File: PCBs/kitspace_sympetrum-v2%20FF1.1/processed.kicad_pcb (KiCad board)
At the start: 2 copper layers, 98.8 x 77.3 mm, 67 parts, among them SW101 DFU, U101 STM32F030K6T6, U102 TSSP58P38, U201 APA102_5050, U202 APA102_5050, U203 APA102_5050, U204 APA102_5050, U205 APA102_5050, U206 APA102_5050, U207 APA102_5050, U208 APA102_5050, U209 APA102_5050, U210 APA102_5050, U301 AAT1217-3.3

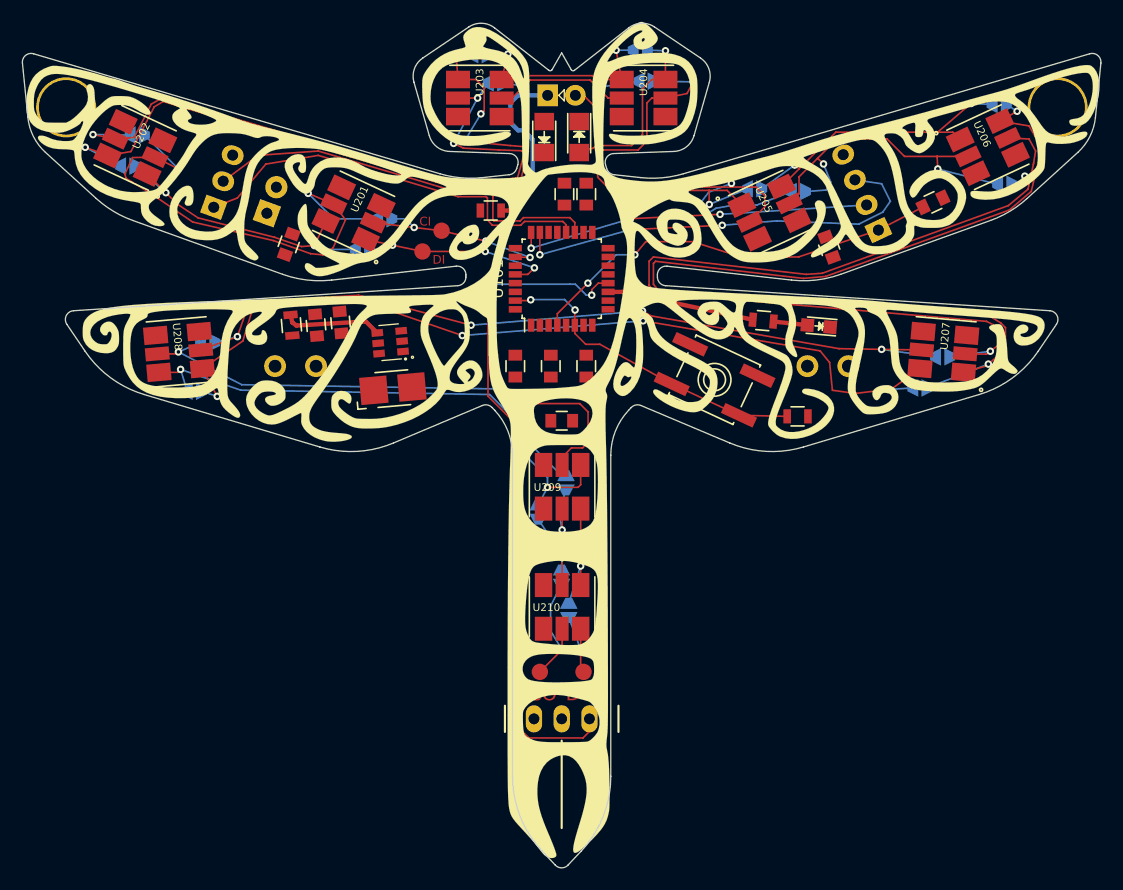
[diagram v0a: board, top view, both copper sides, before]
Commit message: recheck all circuits and clean up fill zone by rerouting the nets using freerouting and manually
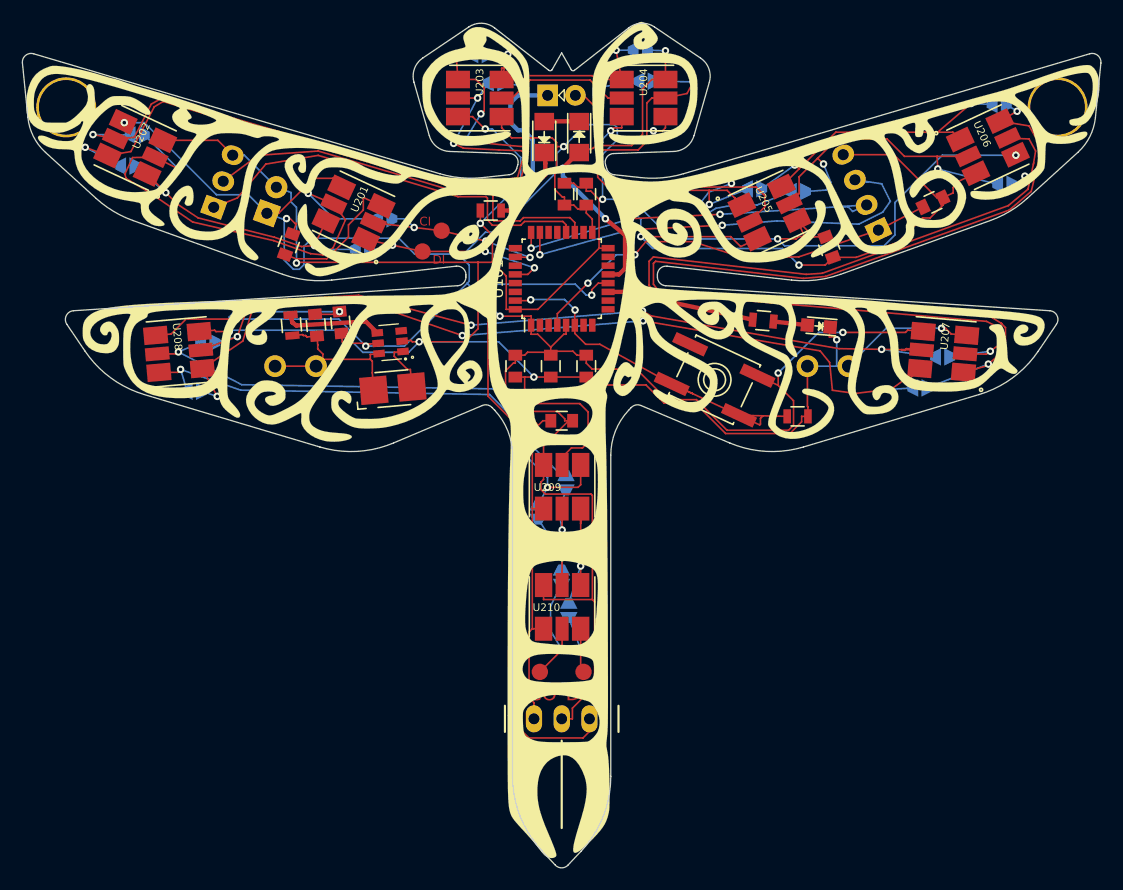
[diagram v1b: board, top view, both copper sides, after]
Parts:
- renumbered G*** to G***_2, G*** to G***_3
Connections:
- B301 pad 1: (no net) -> +BATT
- B301 pad 2: (no net) -> GND
- C101 pad 2: (no net) -> GND
- C102 pad 1: (no net) -> +3V3
- C102 pad 2: (no net) -> GND
- C103 pad 1: (no net) -> +3V3
- C103 pad 2: (no net) -> GND
- C104 pad 1: (no net) -> +3V3
- C104 pad 2: (no net) -> GND
- C105 pad 1: (no net) -> +3V3
- C105 pad 2: (no net) -> GND
- C106 pad 1: (no net) -> +3V3
- C106 pad 2: (no net) -> GND
- C201 pad 1: (no net) -> +3V3
- C201 pad 2: (no net) -> GND
- C202 pad 1: (no net) -> +3V3
- C202 pad 2: (no net) -> GND
- C203 pad 1: (no net) -> +3V3
- C203 pad 2: (no net) -> GND
- C301 pad 1: (no net) -> +BATT
- C301 pad 2: (no net) -> GND
- C302 pad 1: (no net) -> +3V3
- C302 pad 2: (no net) -> GND
- D101 pad 1: (no net) -> GND
- D102 pad 1: (no net) -> Net-(D102-Pad1)
- D103 pad 1: (no net) -> Net-(D103-Pad1)
- D103 pad 2: (no net) -> Net-(D102-Pad1)
- J_PROG101 pad 4: (no net) -> GND
- J_PWR301 pad 1: (no net) -> +3V3
- J_PWR301 pad 2: (no net) -> GND
- J_UART101 pad 3: (no net) -> GND
- L301 pad 1: (no net) -> +BATT
- L301 pad 2: (no net) -> Net-(L301-Pad2)
- R101 pad 2: (no net) -> GND
- R103 pad 1: (no net) -> GND
- R301 pad 1: (no net) -> +BATT
- SW101 pad 1: (no net) -> Net-(SW101-Pad1)
- SW101 pad 3: (no net) -> +3V3
- U101 pad 1: (no net) -> +3V3
- U101 pad 10: (no net) -> Net-(U101-Pad10)
- U101 pad 13: (no net) -> /IR_TX
- U101 pad 14: (no net) -> Net-(U101-Pad14)
- U101 pad 15: (no net) -> Net-(U101-Pad15)
- U101 pad 16: (no net) -> GND
- U101 pad 17: (no net) -> +3V3
- U101 pad 18: (no net) -> Net-(U101-Pad18)
- U101 pad 2: (no net) -> Net-(U101-Pad2)
- U101 pad 21: (no net) -> Net-(U101-Pad21)
- U101 pad 22: (no net) -> Net-(U101-Pad22)
- U101 pad 25: (no net) -> Net-(U101-Pad25)
- U101 pad 27: (no net) -> Net-(U101-Pad27)
- U101 pad 29: (no net) -> Net-(U101-Pad29)
- U101 pad 3: (no net) -> Net-(U101-Pad3)
- U101 pad 30: (no net) -> Net-(U101-Pad30)
- U101 pad 32: (no net) -> GND
- U101 pad 5: (no net) -> +3V3
- U101 pad 7: (no net) -> Net-(U101-Pad7)
- U101 pad 8: (no net) -> Net-(U101-Pad8)
- U101 pad 9: (no net) -> Net-(U101-Pad9)
- U102 pad 2: (no net) -> GND
- U102 pad 3: (no net) -> +3V3
- U201 pad 3: (no net) -> GND
- U201 pad 4: (no net) -> +3V3
- U202 pad 3: (no net) -> GND
- U202 pad 4: (no net) -> +3V3
- U203 pad 3: (no net) -> GND
- U203 pad 4: (no net) -> +3V3
- U204 pad 3: (no net) -> GND
- U204 pad 4: (no net) -> +3V3
- U205 pad 3: (no net) -> GND
- U205 pad 4: (no net) -> +3V3
- U206 pad 3: (no net) -> GND
- U206 pad 4: (no net) -> +3V3
- U207 pad 3: (no net) -> GND
- U207 pad 4: (no net) -> +3V3
- U208 pad 3: (no net) -> GND
- U208 pad 4: (no net) -> +3V3
- U209 pad 3: (no net) -> GND
- U209 pad 4: (no net) -> +3V3
- U210 pad 3: (no net) -> GND
- U210 pad 4: (no net) -> +3V3
- U301 pad 1: (no net) -> Net-(L301-Pad2)
- U301 pad 2: (no net) -> GND
- U301 pad 3: (no net) -> Net-(U301-Pad3)
- U301 pad 5: (no net) -> +3V3
- U301 pad 6: (no net) -> +BATT
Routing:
- net GND: track 0.00 -> 333.6 mm, vias 0 -> 13
- net +3V3: track 0.00 -> 298.9 mm, vias 0 -> 11
- net +BATT: track 0.00 -> 17.8 mm
- net /IR_TX: track 7.97 -> 23.5 mm, vias 0 -> 2
- net /USER_BUTTON: track 29.5 -> 34.6 mm
- net Net-(D103-Pad1): track 16.3 -> 21.3 mm
- net Net-(L301-Pad2): track 0.00 -> 4.76 mm
- net Net-(D102-Pad1): track 0.00 -> 3.22 mm
- net /SWDCLK: track 32.6 -> 35.5 mm
- net Net-(JP213-Pad2): track 11.9 -> 14.2 mm
- net Net-(JP214-Pad2): track 15.4 -> 17.6 mm
- net Net-(JP205-Pad2): track 76.4 -> 78.2 mm
- net Net-(JP206-Pad2): track 79.9 -> 81.7 mm
- net Net-(JP212-Pad2): track 19.9 -> 21.3 mm
- net /SWDIO: track 39.5 -> 40.8 mm
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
